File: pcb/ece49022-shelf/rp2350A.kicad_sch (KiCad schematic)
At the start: 33 parts, among them J1 USB_B_Micro, J4 SM03B-SRSS-TB, SW1 SW_Push, SW2 SW_Push, U3 W25Q128JVS, U5 RP2350_60QFN, Y1 ABM8-272-T3

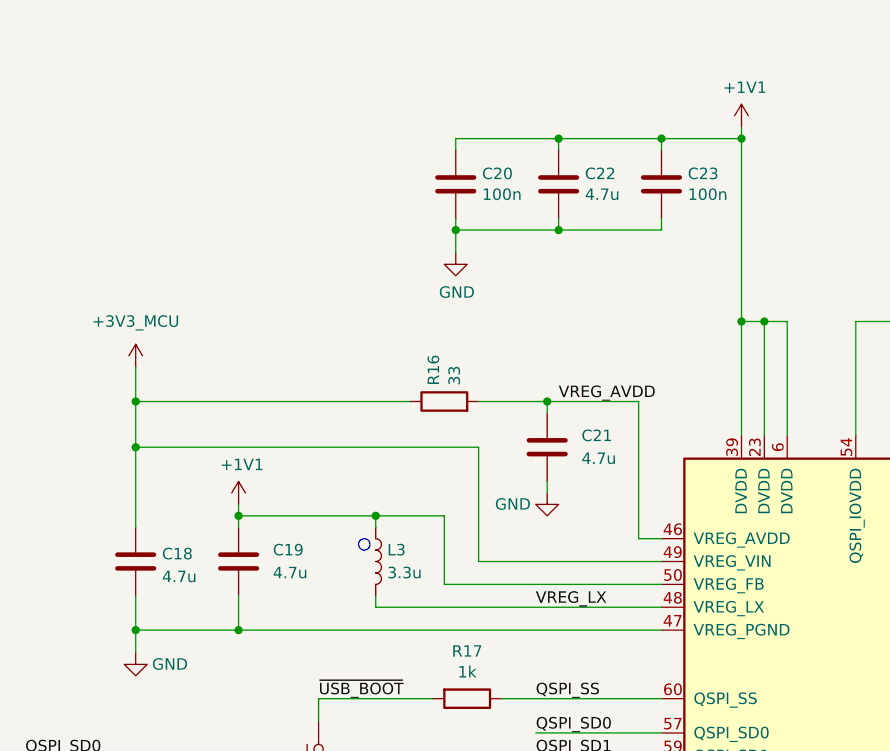
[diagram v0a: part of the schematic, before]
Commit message: start layout and part selection of rp
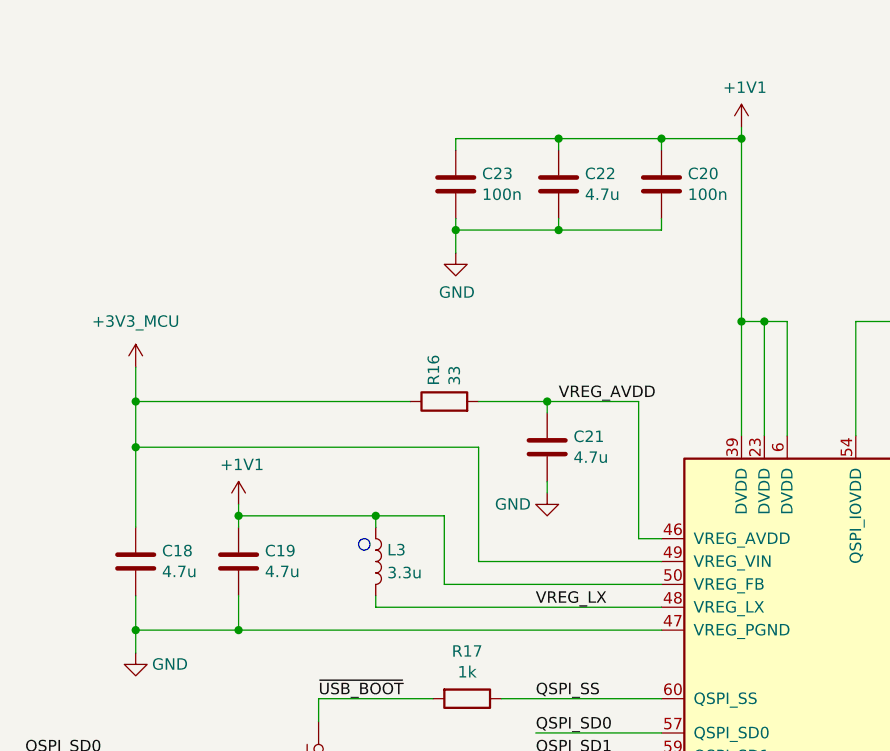
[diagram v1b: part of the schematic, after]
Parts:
- C18, C19, C20, C21, C22, C23, C24, C25, C26, C27, C28, C29, C30: footprint Capacitor_SMD:C_0402_1005Metric -> Capacitor_SMD:C_0402_1005Metric_Pad0.74x0.62mm_HandSolder
- R16: footprint Resistor_SMD:R_0402_1005Metric -> Resistor_SMD:R_0402_1005Metric_Pad0.72x0.64mm_HandSolder

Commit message: stuff
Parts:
- removed H1: MountingHole, MountingHole:MountingHole_2.7mm_M2.5, symbol Mechanical:MountingHole
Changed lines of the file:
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@@
-	)
-	(symbol
-		(lib_id "Mechanical:MountingHole")
-		(at 43.18 224.79 0)
-		(unit 1)
-		(exclude_from_sim no)
-		(in_bom yes)
-		(on_board yes)
-		(dnp no)
-		(property "Reference" "H1"
-			(at 45.72 223.6216 0)
-			(effects
-				(font
-					(size 1.27 1.27)
-				)
-				(justify left)
-			)
-		)
-		(property "Value" "MountingHole"
-			(at 45.72 225.933 0)
-			(effects
-				(font
-					(size 1.27 1.27)
-				)
-				(justify left)
-			)
-		)
-		(property "Footprint" "MountingHole:MountingHole_2.7mm_M2.5"
-			(at 43.18 224.79 0)
-			(effects
-				(font
-					(size 1.27 1.27)
-				)
-				(hide yes)
-			)
-		)
-		(property "Datasheet" "~"
-			(at 43.18 224.79 0)
-			(effects
-				(font
-					(size 1.27 1.27)
-				)
-				(hide yes)
-			)
-		)
-		(property "Description" ""
-			(at 43.18 224.79 0)
-			(effects
-				(font
-					(size 1.27 1.27)
-				)
-			)
-		)
-		(instances
-			(project "ece49022-shelf"
-				(path "/cb6cb1b4-c151-4aa2-8cd7-5430288cfa02/d90a4203-0e8d-4fad-a588-f7d5681a1fb6"
-					(reference "H1")
-					(unit 1)
-				)
-			)
-		)
 	)
 	(symbol

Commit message: cap footprints for MCU smps needed to change
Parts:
- C18, C19: footprint Capacitor_SMD:C_0402_1005Metric_Pad0.74x0.62mm_HandSolder -> Capacitor_SMD:C_0603_1608Metric
- C21, C22: footprint Capacitor_SMD:C_0402_1005Metric_Pad0.74x0.62mm_HandSolder -> Capacitor_SMD:C_0402_1005Metric
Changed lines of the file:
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@@
 			)
 		)
-		(property "Footprint" "Capacitor_SMD:C_0402_1005Metric_Pad0.74x0.62mm_HandSolder"
+		(property "Footprint" "Capacitor_SMD:C_0603_1608Metric"
 			(at 107.6452 102.87 0)
 			(effects
@@
 			)
 		)
-		(property "Footprint" "Capacitor_SMD:C_0402_1005Metric_Pad0.74x0.62mm_HandSolder"
+		(property "Footprint" "Capacitor_SMD:C_0402_1005Metric"
 			(at 154.6352 60.96 0)
 			(effects
@@
 			)
 		)
-		(property "Footprint" "Capacitor_SMD:C_0402_1005Metric_Pad0.74x0.62mm_HandSolder"
+		(property "Footprint" "Capacitor_SMD:C_0402_1005Metric"
 			(at 153.3652 90.17 0)
 			(effects
@@
 			)
 		)
-		(property "Footprint" "Capacitor_SMD:C_0402_1005Metric_Pad0.74x0.62mm_HandSolder"
+		(property "Footprint" "Capacitor_SMD:C_0603_1608Metric"
 			(at 119.0752 102.87 0)
 			(effects

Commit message: stuff
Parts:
- added C33: 100n, Capacitor_SMD:C_0402_1005Metric_Pad0.74x0.62mm_HandSolder, symbol Device:C
- C18, C19: footprint Capacitor_SMD:C_0603_1608Metric -> 49022_Footprints:C_0402_1005Metric_small_pads
- R14: footprint Resistor_SMD:R_0402_1005Metric -> Resistor_SMD:R_0402_1005Metric_Pad0.72x0.64mm_HandSolder
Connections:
- net +1V1: now also C33.1
- net GND: now also C33.2
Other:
- moved on the sheet: C20, C22, C23
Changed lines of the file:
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@@
 	)
 	(junction
-		(at 153.67 52.07)
+		(at 142.24 52.07)
 		(diameter 0)
 		(color 0 0 0 0)
@@
 	)
 	(junction
-		(at 165.1 52.07)
+		(at 153.67 52.07)
 		(diameter 0)
 		(color 0 0 0 0)
@@
 	)
 	(junction
-		(at 142.24 62.23)
+		(at 153.67 62.23)
+		(diameter 0)
+		(color 0 0 0 0)
+	)
+	(junction
+		(at 130.81 62.23)
 		(diameter 0)
 		(color 0 0 0 0)
@@
 	)
 	(junction
-		(at 153.67 62.23)
+		(at 142.24 62.23)
 		(diameter 0)
 		(color 0 0 0 0)
@@
 	)
 	(junction
+		(at 165.1 52.07)
+		(diameter 0)
+		(color 0 0 0 0)
+	)
+	(junction
 		(at 198.12 72.39)
 		(diameter 0)
@@
 	(wire
 		(pts
+			(xy 165.1 52.07) (xy 173.99 52.07)
+		)
+		(stroke
+			(width 0)
+			(type default)
+		)
+	)
+	(wire
+		(pts
 			(xy 213.36 52.07) (xy 213.36 72.39)
 		)
@@
 	(wire
 		(pts
-			(xy 153.67 53.34) (xy 153.67 52.07)
+			(xy 142.24 53.34) (xy 142.24 52.07)
 		)
 		(stroke
@@
 	(wire
 		(pts
-			(xy 142.24 62.23) (xy 142.24 64.77)
+			(xy 130.81 62.23) (xy 130.81 64.77)
 		)
 		(stroke
@@
 	(wire
 		(pts
-			(xy 165.1 62.23) (xy 165.1 60.96)
+			(xy 153.67 62.23) (xy 153.67 60.96)
 		)
 		(stroke
@@
 	(wire
 		(pts
+			(xy 165.1 52.07) (xy 165.1 53.34)
+		)
+		(stroke
+			(width 0)
+			(type default)
+		)
+	)
+	(wire
+		(pts
 			(xy 279.4 52.07) (xy 290.83 52.07)
 		)
@@
 	(wire
 		(pts
-			(xy 165.1 53.34) (xy 165.1 52.07)
+			(xy 153.67 53.34) (xy 153.67 52.07)
 		)
 		(stroke
@@
 	(wire
 		(pts
+			(xy 153.67 62.23) (xy 165.1 62.23)
+		)
+		(stroke
+			(width 0)
+			(type default)
+		)
+	)
+	(wire
+		(pts
 			(xy 45.72 128.27) (xy 60.96 128.27)
 		)
@@
 	(wire
 		(pts
-			(xy 153.67 60.96) (xy 153.67 62.23)
+			(xy 142.24 60.96) (xy 142.24 62.23)
 		)
 		(stroke
@@
 	(wire
 		(pts
-			(xy 142.24 60.96) (xy 142.24 62.23)
+			(xy 130.81 60.96) (xy 130.81 62.23)
 		)
 		(stroke
@@
 	(wire
 		(pts
-			(xy 165.1 52.07) (xy 173.99 52.07)
+			(xy 153.67 52.07) (xy 165.1 52.07)
 		)
 		(stroke
@@
 	(wire
 		(pts
-			(xy 153.67 62.23) (xy 165.1 62.23)
+			(xy 142.24 62.23) (xy 153.67 62.23)
 		)
 		(stroke
@@
 	(wire
 		(pts
-			(xy 142.24 52.07) (xy 153.67 52.07)
+			(xy 130.81 52.07) (xy 142.24 52.07)
 		)
 		(stroke
@@
 	(wire
 		(pts
+			(xy 165.1 60.96) (xy 165.1 62.23)
+		)
+		(stroke
+			(width 0)
+			(type default)
+		)
+	)
+	(wire
+		(pts
 			(xy 127 114.3) (xy 127 116.84)
 		)
@@
 	(wire
 		(pts
-			(xy 153.67 52.07) (xy 165.1 52.07)
+			(xy 142.24 52.07) (xy 153.67 52.07)
 		)
 		(stroke
@@
 	(wire
 		(pts
-			(xy 142.24 53.34) (xy 142.24 52.07)
+			(xy 130.81 53.34) (xy 130.81 52.07)
 		)
 		(stroke
@@
 	(wire
 		(pts
-			(xy 142.24 62.23) (xy 153.67 62.23)
+			(xy 130.81 62.23) (xy 142.24 62.23)
 		)
 		(stroke
@@
 	(symbol
 		(lib_id "Device:C")
-		(at 142.24 57.15 0)
+		(at 130.81 57.15 0)
 		(unit 1)
 		(exclude_from_sim no)
@@
 		(dnp no)
 		(property "Reference" "C23"
-			(at 145.161 55.9816 0)
+			(at 133.731 55.9816 0)
 			(effects
 				(font
@@
 		)
 		(property "Value" "100n"
-			(at 145.161 58.293 0)
+			(at 133.731 58.293 0)
 			(effects
 				(font
@@
 		)
 		(property "Footprint" "Capacitor_SMD:C_0402_1005Metric_Pad0.74x0.62mm_HandSolder"
-			(at 143.2052 60.96 0)
+			(at 131.7752 60.96 0)
 			(effects
 				(font
@@
 		)
 		(property "Datasheet" "~"
-			(at 142.24 57.15 0)
+			(at 130.81 57.15 0)
 			(effects
 				(font
@@
 		)
 		(property "Description" "CC0402KRX5R9BB104"
-			(at 142.24 57.15 0)
+			(at 130.81 57.15 0)
 			(effects
 				(font
@@
 			)
 		)
-		(property "Footprint" "Capacitor_SMD:C_0603_1608Metric"
+		(property "Footprint" "49022_Footprints:C_0402_1005Metric_small_pads"
 			(at 107.6452 102.87 0)
 			(effects
@@
 			)
 		)
-		(property "Footprint" "Resistor_SMD:R_0402_1005Metric"
+		(property "Footprint" "Resistor_SMD:R_0402_1005Metric_Pad0.72x0.64mm_HandSolder"
 			(at 82.55 198.882 90)
 			(effects
@@
 	(symbol
 		(lib_id "Device:C")
-		(at 165.1 57.15 0)
+		(at 153.67 57.15 0)
 		(unit 1)
 		(exclude_from_sim no)
@@
 		(dnp no)
 		(property "Reference" "C20"
-			(at 168.021 55.9816 0)
+			(at 156.591 55.9816 0)
 			(effects
 				(font
@@
 		)
 		(property "Value" "100n"
-			(at 168.021 58.293 0)
+			(at 156.591 58.293 0)
 			(effects
 				(font
@@
 		)
 		(property "Footprint" "Capacitor_SMD:C_0402_1005Metric_Pad0.74x0.62mm_HandSolder"
-			(at 166.0652 60.96 0)
+			(at 154.6352 60.96 0)
 			(effects
 				(font
@@
 		)
 		(property "Datasheet" "~"
-			(at 165.1 57.15 0)
+			(at 153.67 57.15 0)
 			(effects
 				(font
@@
 		)
 		(property "Description" "CC0402KRX5R9BB104"
-			(at 165.1 57.15 0)
+			(at 153.67 57.15 0)
 			(effects
 				(font
@@
 	(symbol
 		(lib_id "Device:C")
-		(at 153.67 57.15 0)
+		(at 142.24 57.15 0)
 		(unit 1)
 		(exclude_from_sim no)
@@
 		(dnp no)
 		(property "Reference" "C22"
-			(at 156.591 55.9816 0)
+			(at 145.161 55.9816 0)
 			(effects
 				(font
@@
 		)
 		(property "Value" "4.7u"
-			(at 156.591 58.293 0)
+			(at 145.161 58.293 0)
 			(effects
 				(font
@@
 		)
 		(property "Footprint" "Capacitor_SMD:C_0402_1005Metric"
-			(at 154.6352 60.96 0)
+			(at 143.2052 60.96 0)
 			(effects
 				(font
@@
 		)
 		(property "Datasheet" "~"
-			(at 153.67 57.15 0)
+			(at 142.24 57.15 0)
 			(effects
 				(font
@@
 		)
 		(property "Description" "CC0402MRX5R6BB475"
-			(at 153.67 57.15 0)
+			(at 142.24 57.15 0)
 			(effects
 				(font
@@
 	(symbol
 		(lib_id "power:GND")
-		(at 142.24 64.77 0)
+		(at 130.81 64.77 0)
 		(unit 1)
 		(exclude_from_sim no)
@@
 		(dnp no)
 		(property "Reference" "#PWR031"
-			(at 142.24 71.12 0)
+			(at 130.81 71.12 0)
 			(effects
 				(font
@@
 		)
 		(property "Value" "GND"
-			(at 142.367 69.1642 0)
+			(at 130.937 69.1642 0)
 			(effects
 				(font
@@
 		)
 		(property "Footprint" ""
-			(at 142.24 64.77 0)
+			(at 130.81 64.77 0)
 			(effects
 				(font
@@
 		)
 		(property "Datasheet" ""
-			(at 142.24 64.77 0)
+			(at 130.81 64.77 0)
 			(effects
 				(font
@@
 		)
 		(property "Description" ""
-			(at 142.24 64.77 0)
+			(at 130.81 64.77 0)
 			(effects
 				(font
@@
 	)
 	(symbol
+		(lib_id "Device:C")
+		(at 165.1 57.15 0)
+		(unit 1)
+		(exclude_from_sim no)
+		(in_bom yes)
+		(on_board yes)
+		(dnp no)
+		(property "Reference" "C33"
+			(at 168.021 55.9816 0)
+			(effects
+				(font
+					(size 1.27 1.27)
+				)
+				(justify left)
+			)
+		)
+		(property "Value" "100n"
+			(at 168.021 58.293 0)
+			(effects
+				(font
+					(size 1.27 1.27)
+				)
+				(justify left)
+			)
+		)
+		(property "Footprint" "Capacitor_SMD:C_0402_1005Metric_Pad0.74x0.62mm_HandSolder"
+			(at 166.0652 60.96 0)
+			(effects
+				(font
+					(size 1.27 1.27)
+				)
+				(hide yes)
+			)
+		)
+		(property "Datasheet" "~"
+			(at 165.1 57.15 0)
+			(effects
+				(font
+					(size 1.27 1.27)
+				)
+				(hide yes)
+			)
+		)
+		(property "Description" "CC0402KRX5R9BB104"
+			(at 165.1 57.15 0)
+			(effects
+				(font
+					(size 1.27 1.27)
+				)
+				(hide yes)
+			)
+		)
+		(pin "1"
+		)
+		(pin "2"
+		)
+		(instances
+			(project "ece49022-shelf"
+				(path "/cb6cb1b4-c151-4aa2-8cd7-5430288cfa02/d90a4203-0e8d-4fad-a588-f7d5681a1fb6"
+					(reference "C33")
+					(unit 1)
+				)
+			)
+		)
+	)
+	(symbol
 		(lib_id "power:GND")
 		(at 80.01 109.22 0)
@@
 			)
 		)
-		(property "Footprint" "Capacitor_SMD:C_0603_1608Metric"
+		(property "Footprint" "49022_Footprints:C_0402_1005Metric_small_pads"
 			(at 119.0752 102.87 0)
 			(effects

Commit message: routing
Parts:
- removed C33: 100n, Capacitor_SMD:C_0402_1005Metric_Pad0.74x0.62mm_HandSolder, symbol Device:C
- C21, C22: footprint Capacitor_SMD:C_0402_1005Metric -> Capacitor_SMD:C_0402_1005Metric_Pad0.74x0.62mm_HandSolder
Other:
- moved on the sheet: C20, C22, C23

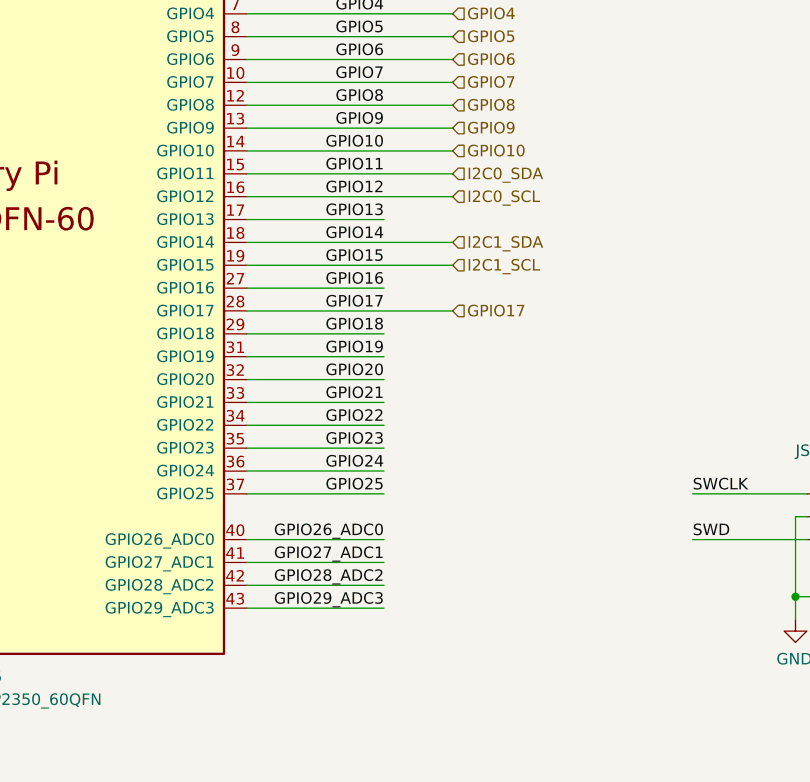
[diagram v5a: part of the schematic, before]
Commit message: edited nau7802 schem and changed pins for layout reasons
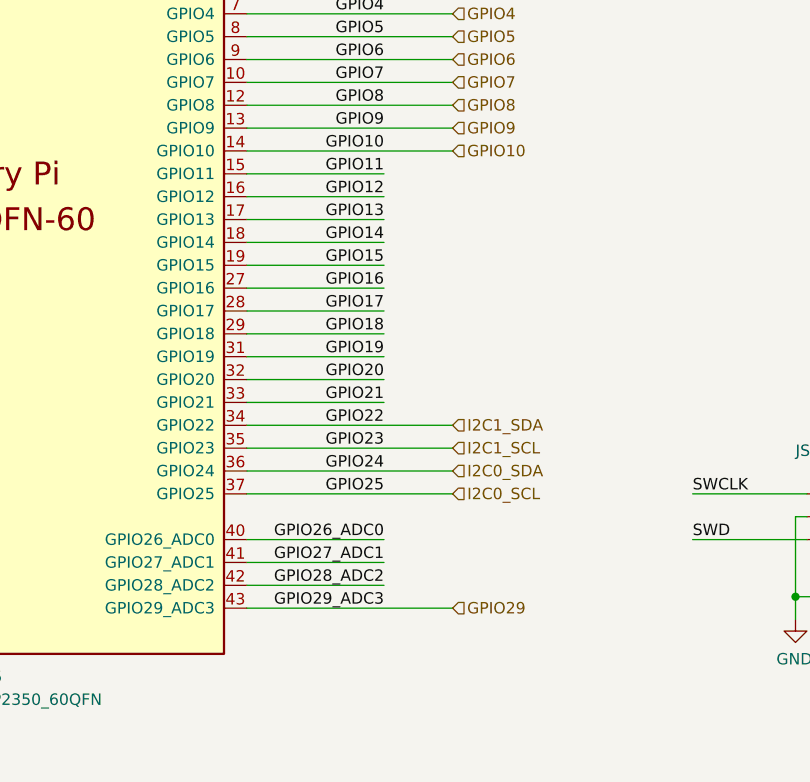
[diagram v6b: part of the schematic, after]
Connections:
- net GPIO22 is gone; now on net I2C1_SDA: U5.34 (GPIO22)
- net GPIO23 is gone; now on net I2C1_SCL: U5.35 (GPIO23)
- net GPIO24 is gone; now on net I2C0_SDA: U5.36 (GPIO24)
- net GPIO25 is gone; now on net I2C0_SCL: U5.37 (GPIO25)
- net I2C0_SCL: no longer U5.16 (GPIO12)
- net I2C0_SDA: no longer U5.15 (GPIO11)
- net I2C1_SCL: no longer U5.19 (GPIO15)
- net I2C1_SDA: no longer U5.18 (GPIO14)
- net GPIO29_ADC3 renamed GPIO29
- new net GPIO11: U5.15 (GPIO11)
- new net GPIO12: U5.16 (GPIO12)
- new net GPIO14: U5.18 (GPIO14)
- new net GPIO15: U5.19 (GPIO15)
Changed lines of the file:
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@@
-	(wire
-		(pts
-			(xy 228.6 161.29) (xy 243.84 161.29)
-		)
-		(stroke
-			(width 0)
-			(type default)
-		)
-	)
 	(wire
 		(pts
@@
 	(wire
 		(pts
+			(xy 228.6 161.29) (xy 251.46 161.29)
+		)
+		(stroke
+			(width 0)
+			(type default)
+		)
+	)
+	(wire
+		(pts
 			(xy 133.35 104.14) (xy 165.1 104.14)
 		)
@@
 	(wire
 		(pts
-			(xy 228.6 146.05) (xy 251.46 146.05)
-		)
-		(stroke
-			(width 0)
-			(type default)
-		)
-	)
-	(wire
-		(pts
 			(xy 64.77 191.77) (xy 64.77 190.5)
 		)
@@
 	(wire
 		(pts
-			(xy 228.6 158.75) (xy 243.84 158.75)
-		)
-		(stroke
-			(width 0)
-			(type default)
-		)
-	)
-	(wire
-		(pts
 			(xy 118.11 102.87) (xy 118.11 106.68)
 		)
@@
 	(wire
 		(pts
-			(xy 228.6 130.81) (xy 251.46 130.81)
+			(xy 228.6 158.75) (xy 251.46 158.75)
 		)
 		(stroke
@@
 	(wire
 		(pts
+			(xy 228.6 163.83) (xy 251.46 163.83)
+		)
+		(stroke
+			(width 0)
+			(type default)
+		)
+	)
+	(wire
+		(pts
 			(xy 233.68 60.96) (xy 233.68 63.5)
 		)
@@
 	(wire
 		(pts
+			(xy 228.6 133.35) (xy 243.84 133.35)
+		)
+		(stroke
+			(width 0)
+			(type default)
+		)
+	)
+	(wire
+		(pts
 			(xy 228.6 115.57) (xy 251.46 115.57)
 		)
@@
 	(wire
 		(pts
-			(xy 228.6 166.37) (xy 243.84 166.37)
-		)
-		(stroke
-			(width 0)
-			(type default)
-		)
-	)
-	(wire
-		(pts
 			(xy 127 127) (xy 127 129.54)
 		)
@@
 	(wire
 		(pts
-			(xy 228.6 133.35) (xy 251.46 133.35)
-		)
-		(stroke
-			(width 0)
-			(type default)
-		)
-	)
-	(wire
-		(pts
 			(xy 228.6 171.45) (xy 243.84 171.45)
 		)
@@
 	(wire
 		(pts
-			(xy 228.6 163.83) (xy 243.84 163.83)
-		)
-		(stroke
-			(width 0)
-			(type default)
-		)
-	)
-	(wire
-		(pts
 			(xy 64.77 200.66) (xy 78.74 200.66)
 		)
@@
 	(wire
 		(pts
+			(xy 228.6 130.81) (xy 243.84 130.81)
+		)
+		(stroke
+			(width 0)
+			(type default)
+		)
+	)
+	(wire
+		(pts
+			(xy 228.6 138.43) (xy 243.84 138.43)
+		)
+		(stroke
+			(width 0)
+			(type default)
+		)
+	)
+	(wire
+		(pts
 			(xy 144.78 99.06) (xy 165.1 99.06)
 		)
@@
 	(wire
 		(pts
-			(xy 228.6 179.07) (xy 243.84 179.07)
+			(xy 228.6 179.07) (xy 251.46 179.07)
 		)
 		(stroke
@@
 	(wire
 		(pts
+			(xy 228.6 166.37) (xy 251.46 166.37)
+		)
+		(stroke
+			(width 0)
+			(type default)
+		)
+	)
+	(wire
+		(pts
 			(xy 279.4 60.96) (xy 279.4 63.5)
 		)
@@
 	(wire
 		(pts
+			(xy 228.6 140.97) (xy 243.84 140.97)
+		)
+		(stroke
+			(width 0)
+			(type default)
+		)
+	)
+	(wire
+		(pts
 			(xy 151.13 120.65) (xy 165.1 120.65)
 		)
@@
 	(wire
 		(pts
-			(xy 228.6 140.97) (xy 251.46 140.97)
-		)
-		(stroke
-			(width 0)
-			(type default)
-		)
-	)
-	(wire
-		(pts
 			(xy 245.11 60.96) (xy 245.11 63.5)
 		)
@@
 	(wire
 		(pts
-			(xy 228.6 138.43) (xy 251.46 138.43)
-		)
-		(stroke
-			(width 0)
-			(type default)
-		)
-	)
-	(wire
-		(pts
 			(xy 278.13 166.37) (xy 290.83 166.37)
 		)
@@
 		(pts
 			(xy 205.74 72.39) (xy 209.55 72.39)
+		)
+		(stroke
+			(width 0)
+			(type default)
+		)
+	)
+	(wire
+		(pts
+			(xy 228.6 146.05) (xy 243.84 146.05)
 		)
 		(stroke
@@
 		)
 	)
-	(hierarchical_label "GPIO17"
+	(hierarchical_label "GPIO29"
 		(shape input)
-		(at 251.46 146.05 0)
+		(at 251.46 179.07 0)
 		(effects
 			(font
@@
 		)
 	)
-	(hierarchical_label "I2C1_SDA"
+	(hierarchical_label "I2C0_SCL"
 		(shape input)
-		(at 251.46 138.43 0)
+		(at 251.46 166.37 0)
 		(effects
 			(font
@@
 		)
 	)
+	(hierarchical_label "I2C1_SDA"
+		(shape input)
+		(at 251.46 158.75 0)
+		(effects
+			(font
+				(size 1.27 1.27)
+			)
+			(justify left)
+		)
+	)
 	(hierarchical_label "+3V3"
 		(shape input)
@@
 		)
 	)
-	(hierarchical_label "I2C1_SCL"
-		(shape input)
-		(at 251.46 140.97 0)
-		(effects
-			(font
-				(size 1.27 1.27)
-			)
-			(justify left)
-		)
-	)
 	(hierarchical_label "GPIO4"
 		(shape input)
@@
 		)
 	)
-	(hierarchical_label "I2C0_SCL"
+	(hierarchical_label "I2C0_SDA"
 		(shape input)
-		(at 251.46 133.35 0)
+		(at 251.46 163.83 0)
 		(effects
 			(font
@@
 		)
 	)
+	(hierarchical_label "I2C1_SCL"
+		(shape input)
+		(at 251.46 161.29 0)
+		(effects
+			(font
+				(size 1.27 1.27)
+			)
+			(justify left)
+		)
+	)
 	(hierarchical_label "GPIO10"
 		(shape input)
@@
 		(effects
 			(font
-				(size 1.27 1.27)
-			)
-			(justify left)
-		)
-	)
-	(hierarchical_label "I2C0_SDA"
-		(shape input)
-		(at 251.46 130.81 0)
-		(effects
-			(font
